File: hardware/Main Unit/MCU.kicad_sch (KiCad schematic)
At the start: 40 parts, among them J1 3221-10-0300-00, J12 USB4105-GF-A, SW1 MJTP1243, SW2 MJTP1243, U1 MCXN547VKLT, U13 USBLC6-2SC6, X1 24.0000MHz

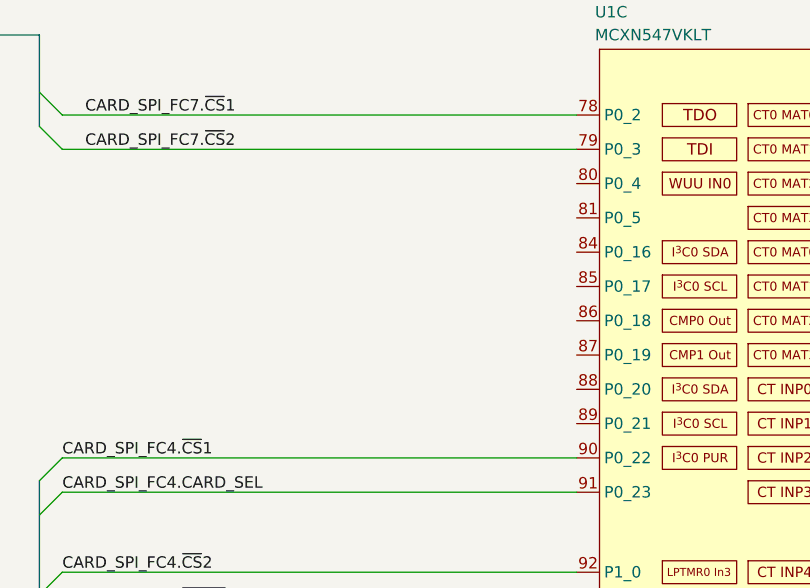
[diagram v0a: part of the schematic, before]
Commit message: Route more of main unit, start on KiBot CI job
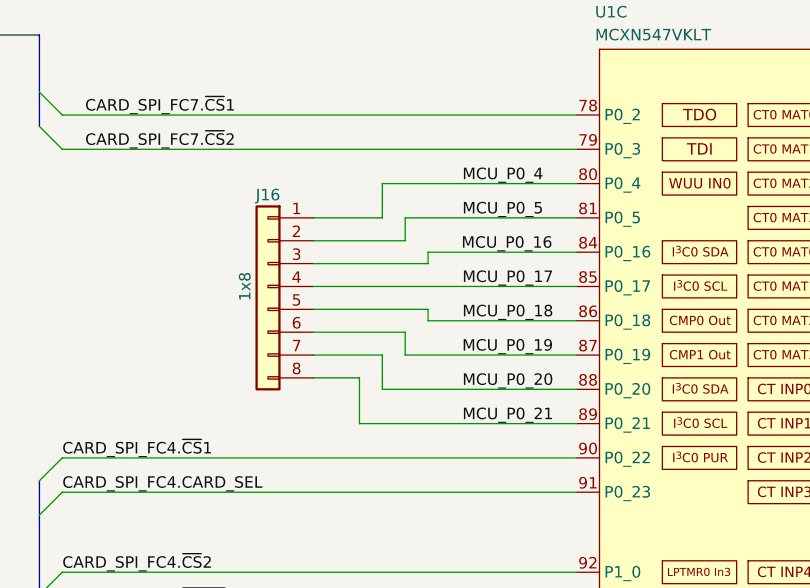
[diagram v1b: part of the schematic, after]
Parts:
- added J16: 1x8, Connector_PinSocket_2.54mm:PinSocket_1x08_P2.54mm_Vertical, symbol Connector_Generic:Conn_01x08
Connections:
- net MCU_P0_4: now reaches U1.80 (P0_4)
- net MCU_P0_4: now also J16.1 (Pin_1)
- net MCU_P0_5: now reaches U1.81 (P0_5)
- net MCU_P0_5: now also J16.2 (Pin_2)
- net MCU_P0_16: now reaches U1.84 (P0_16)
- net MCU_P0_16: now also J16.3 (Pin_3)
- net MCU_P0_17: now reaches U1.85 (P0_17)
- net MCU_P0_17: now also J16.4 (Pin_4)
- net MCU_P0_18: now reaches U1.86 (P0_18)
- net MCU_P0_18: now also J16.5 (Pin_5)
- net MCU_P0_19: now reaches U1.87 (P0_19)
- net MCU_P0_19: now also J16.6 (Pin_6)
- net MCU_P0_20: now reaches U1.88 (P0_20)
- net MCU_P0_20: now also J16.7 (Pin_7)
- net MCU_P0_21: now reaches U1.89 (P0_21)
- net MCU_P0_21: now also J16.8 (Pin_8)

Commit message: Add LEDs and 5V regulator to main unit
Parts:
- added D10: AA3528SURSK, ColorLEDs:AA3528, symbol ColorLEDs:AA3528SURSK
- added D11: AA3528QBS, ColorLEDs:AA3528, symbol ColorLEDs:AA3528QBS
- added D9: ASMB-MTB0-0A3A2, LED_SMD:LED_Avago_PLCC4_3.2x2.8mm_CW, symbol LED:ASMB-MTB0-0A3A2
- added R55, R56, R58: 30, Resistor_SMD:R_0603_1608Metric, symbol Device:R_Small_US
- added R57, R59: 140, Resistor_SMD:R_0603_1608Metric, symbol Device:R_Small_US
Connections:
- net +3.3V: now also D9.1 (A)
- net +3.3V_CUR_SENSE: now also U1.22 (P4_0); no longer U1.37 (P4_15)
- net +5V_CUR_SENSE: now also U1.23 (P4_1); no longer U1.38 (P4_16)
- net GND: now also D10.1 (K), D11.1 (K)
- net V_{SUPPLY}_CUR_SENSE: now also U1.24 (P4_2); no longer U1.39 (P4_17)
- net STATUS_LED: now reaches U1.25 (P4_3)
- net STATUS_LED: now also R58.1
- net ERROR_LED: now reaches U1.26 (P4_4)
- net ERROR_LED: now also R59.2
- new net: D9.2 (BK), R55.1
- new net: D9.3 (GK), R56.1
- new net: D9.4 (RK), R57.1
- new net: D10.2 (A), R59.1
- new net: D11.2 (A), R58.2
- new net RGB_LED_~{B}: R57.2, U1.39 (P4_17)
- new net RGB_LED_~{G}: R56.2, U1.38 (P4_16)
- new net RGB_LED_~{R}: R55.2, U1.37 (P4_15)
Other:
- note added: "Expansion Header"

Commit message: Main board routed!!
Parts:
- D9: value ASMB-MTB0-0A3A2 -> ASMB-MTB0-0B3A2; footprint LED_SMD:LED_Avago_PLCC4_3.2x2.8mm_CW -> ColorLEDs:LED_Avago_PLCC4_3.2x2.8mm_CW_Fixed3DModel; SKU (none) -> 516-ASMB-MTB0-0B3A2CT-ND; Supplier (none) -> Digi-Key
- X1: footprint Oscillator:Oscillator_SMD_ECS_2520MV-xxx-xx-4Pin_2.5x2.0mm -> Project Library:Oscillator_SMD_ECS_2520MV-xxx-xx-4Pin_2.5x2.0mm_Fixed3DModel
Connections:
- net RGB_LED_~{B}: now also R55.2; no longer R57.2
- net RGB_LED_~{R}: now also R57.2; no longer R55.2
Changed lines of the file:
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@@
 		(exclude_from_sim no)
 		(at 196.85 500.38 0)
-		(size 38.1 19.05)
+		(size 38.1 15.24)
 		(margins 0.9525 0.9525 0.9525 0.9525)
 		(stroke
@@
 	(wire
 		(pts
-			(xy 252.73 511.81) (xy 349.25 511.81)
-		)
-		(stroke
-			(width 0)
-			(type default)
-		)
-	)
-	(wire
-		(pts
 			(xy 273.05 328.93) (xy 353.06 328.93)
 		)
@@
 	(wire
 		(pts
-			(xy 242.57 519.43) (xy 349.25 519.43)
+			(xy 242.57 500.38) (xy 242.57 511.81)
 		)
 		(stroke
@@
 	(wire
 		(pts
-			(xy 252.73 500.38) (xy 252.73 511.81)
-		)
-		(stroke
-			(width 0)
-			(type default)
-		)
-	)
-	(wire
-		(pts
 			(xy 92.71 271.78) (xy 92.71 276.86)
 		)
@@
 	(wire
 		(pts
-			(xy 242.57 500.38) (xy 242.57 519.43)
-		)
-		(stroke
-			(width 0)
-			(type default)
-		)
-	)
-	(wire
-		(pts
 			(xy 67.31 328.93) (xy 74.93 328.93)
 		)
@@
 	(wire
 		(pts
+			(xy 247.65 506.73) (xy 247.65 515.62)
+		)
+		(stroke
+			(width 0)
+			(type default)
+		)
+	)
+	(wire
+		(pts
 			(xy 308.61 488.95) (xy 349.25 488.95)
 		)
@@
 	(wire
 		(pts
+			(xy 242.57 511.81) (xy 349.25 511.81)
+		)
+		(stroke
+			(width 0)
+			(type default)
+		)
+	)
+	(wire
+		(pts
 			(xy 74.93 130.81) (xy 74.93 132.08)
 		)
@@
 	(wire
 		(pts
-			(xy 247.65 506.73) (xy 247.65 515.62)
-		)
-		(stroke
-			(width 0)
-			(type default)
-		)
-	)
-	(wire
-		(pts
 			(xy 87.63 151.13) (xy 87.63 153.67)
 		)
@@
 	(wire
 		(pts
+			(xy 252.73 500.38) (xy 252.73 519.43)
+		)
+		(stroke
+			(width 0)
+			(type default)
+		)
+	)
+	(wire
+		(pts
 			(xy 316.23 298.45) (xy 353.06 298.45)
 		)
@@
 		)
 	)
+	(wire
+		(pts
+			(xy 252.73 519.43) (xy 349.25 519.43)
+		)
+		(stroke
+			(width 0)
+			(type default)
+		)
+	)
 	(bus
 		(pts
@@
 			)
 		)
-		(property "Value" "ASMB-MTB0-0A3A2"
+		(property "Value" "ASMB-MTB0-0B3A2"
 			(at 237.49 488.9499 90)
 			(effects
@@
 			)
 		)
-		(property "Footprint" "LED_SMD:LED_Avago_PLCC4_3.2x2.8mm_CW"
+		(property "Footprint" "ColorLEDs:LED_Avago_PLCC4_3.2x2.8mm_CW_Fixed3DModel"
 			(at 234.95 487.68 0)
 			(effects
@@
 			)
 		)
-		(property "Description" "Tricolor Black Surface LED, Common Anode Pin 1, PLCC-4"
+		(property "Description" "Tricolor Black Surface LED, 20mA, Common Anode Pin 1, PLCC-4"
 			(at 247.65 487.68 0)
 			(effects
@@
 			)
 		)
+		(property "Supplier" "Digi-Key"
+			(at 247.65 487.68 90)
+			(effects
+				(font
+					(size 1.27 1.27)
+				)
+				(hide yes)
+			)
+		)
+		(property "SKU" "516-ASMB-MTB0-0B3A2CT-ND"
+			(at 247.65 487.68 90)
+			(effects
+				(font
+					(size 1.27 1.27)
+				)
+				(hide yes)
+			)
+		)
 		(pin "4"
 		)
@@
 			)
 		)
-		(property "Footprint" "Oscillator:Oscillator_SMD_ECS_2520MV-xxx-xx-4Pin_2.5x2.0mm"
+		(property "Footprint" "Project Library:Oscillator_SMD_ECS_2520MV-xxx-xx-4Pin_2.5x2.0mm_Fixed3DModel"
 			(at 58.42 227.33 0)
 			(effects

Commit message: Geographical reannotate
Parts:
- renumbered C11 to C10, C18 to C11, C15 to C12, C16 to C13, C24 to C14, C12 to C15, C27 to C16, C6 to C17, C21 to C18, C13 to C19, C8 to C20, C9 to C22, C7 to C23, C5 to C24, C4 to C25, C20 to C34, C19 to C5, C14 to C6, C3 to C7, C17 to C8, C10 to C9, D11 to D1, D10 to D2, D9 to D3, D1 to D4, D2 to D5, J16 to J10, J12 to J15, R58 to R1, R18 to R16, R59 to R2, R2 to R23, R57 to R3, R56 to R4, R41 to R44, R42 to R45, R4 to R5, R3 to R6, R55 to R7, R23 to R8, R1 to R9, TP1 to TP2, U13 to U11, U1 to U4
